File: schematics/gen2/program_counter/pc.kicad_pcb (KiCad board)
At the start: 2 copper layers, 100 x 91 mm, 18 parts, among them U1 74HC00, U2 74HC193, U3 74HC193, U4 74HC193, U5 74HC193, U6 74HC245, U7 74HC245

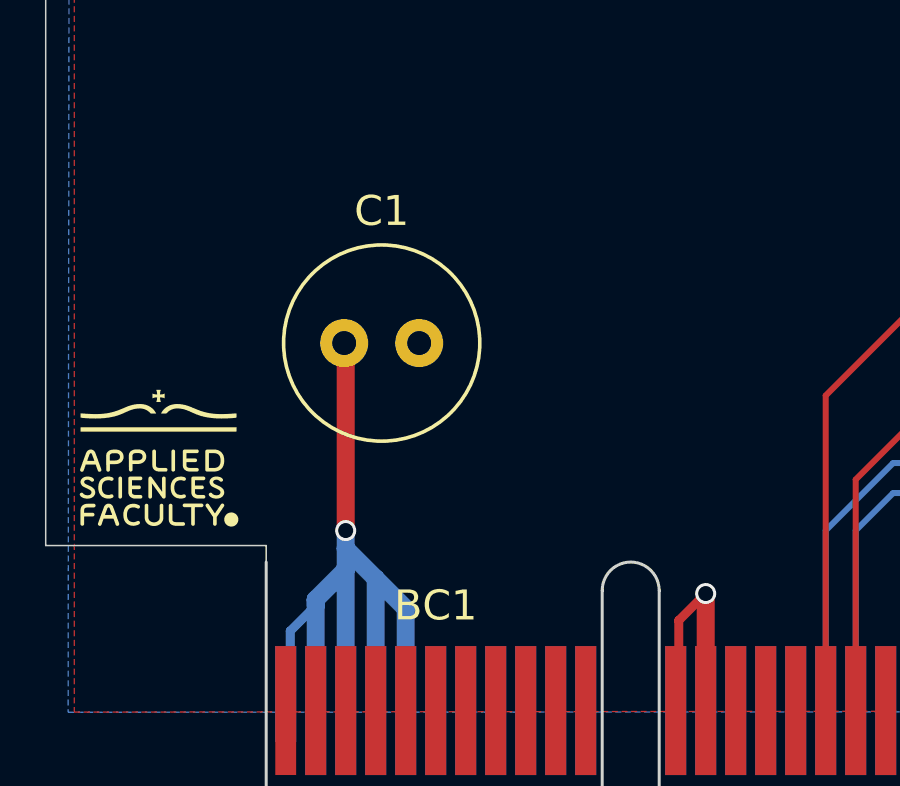
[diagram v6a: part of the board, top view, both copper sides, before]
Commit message: changes pc sc interface
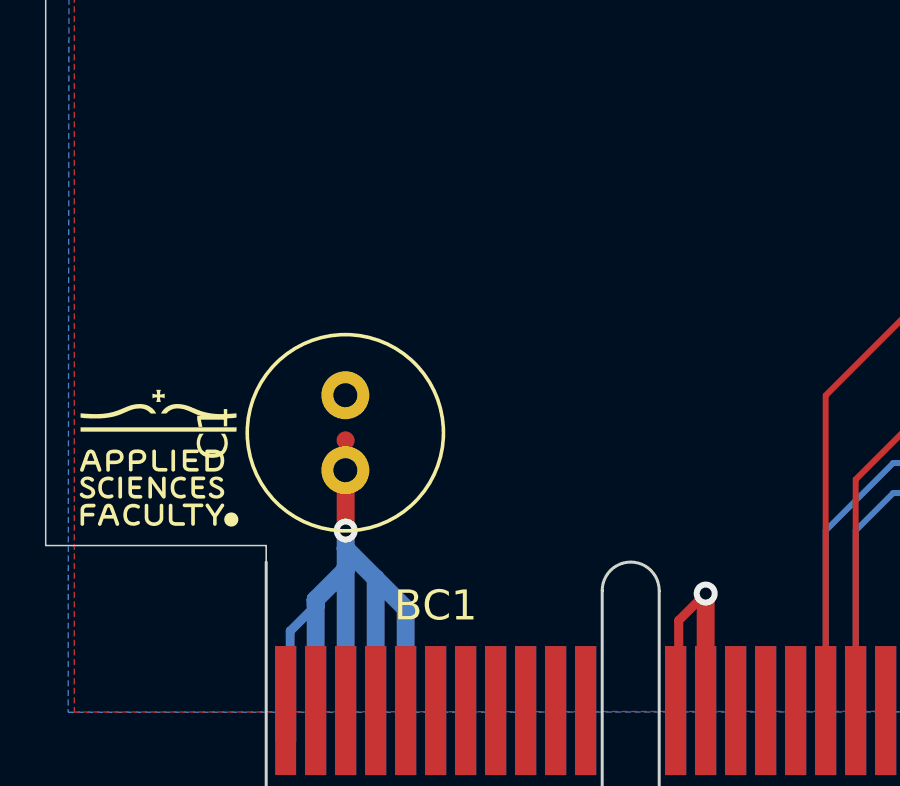
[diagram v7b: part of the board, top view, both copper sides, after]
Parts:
- moved C1 4.24 mm to (116.5, 122.0), turned to 90 degrees
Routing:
- net VCC: track 89.5 -> 85.3 mm
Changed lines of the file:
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@@
 			(pinfunction "VCC")
 			(pintype "power_in")
+			(zone_connect 0)
 		)
 		(embedded_fonts no)
@@
 			(pinfunction "VCC")
 			(pintype "power_in")
+			(zone_connect 0)
 		)
 		(embedded_fonts no)
@@
 			(pinfunction "VCC")
 			(pintype "power_in")
+			(zone_connect 0)
 		)
 		(embedded_fonts no)
@@
 			(pinfunction "VCC")
 			(pintype "power_in")
+			(zone_connect 0)
 		)
 		(embedded_fonts no)
@@
 			(pinfunction "VCC")
 			(pintype "power_in")
+			(zone_connect 0)
 		)
 		(embedded_fonts no)
@@
 			(pinfunction "VCC")
 			(pintype "power_in")
+			(zone_connect 0)
 		)
 		(embedded_fonts no)
@@
 			(pinfunction "VCC")
 			(pintype "power_in")
+			(zone_connect 0)
 		)
 		(embedded_fonts no)
@@
 	(footprint "Capacitor_THT:C_Radial_D6.3mm_H5.0mm_P2.50mm"
 		(layer "F.Cu")
-		(at 116.45 117.75)
+		(at 116.488491 121.98901 90)
 		(descr "C, Radial series, Radial, pin pitch=2.50mm, diameter=6.3mm, height=5mm, Non-Polar Electrolytic Capacitor")
 		(tags "C Radial series Radial pin pitch 2.50mm diameter 6.3mm height 5mm Non-Polar Electrolytic Capacitor")
 		(property "Reference" "C1"
-			(at 1.25 -4.4 0)
+			(at 1.25 -4.4 90)
 			(layer "F.SilkS")
 			(effects
@@
 		)
 		(property "Value" "C"
-			(at 1.25 4.4 0)
+			(at 1.25 4.4 90)
 			(layer "F.Fab")
 			(effects
@@
 		)
 		(property "Datasheet" "~"
-			(at 0 0 0)
+			(at 0 0 90)
 			(layer "F.Fab")
 			(hide yes)
@@
 		)
 		(property "Description" "Unpolarized capacitor"
-			(at 0 0 0)
+			(at 0 0 90)
 			(layer "F.Fab")
 			(hide yes)
@@
 		)
 		(fp_text user "${REFERENCE}"
-			(at 1.25 0 0)
+			(at 1.25 0 90)
 			(layer "F.Fab")
 			(effects
@@
 		)
 		(pad "1" thru_hole circle
-			(at 0 0)
+			(at 0 0 90)
 			(size 1.6 1.6)
 			(drill 0.8)
@@
 		)
 		(pad "2" thru_hole circle
-			(at 2.5 0)
+			(at 2.5 0 90)
 			(size 1.6 1.6)
 			(drill 0.8)
@@
 	)
 	(segment
+		(start 116.5 124)
+		(end 116.5 122.000519)
+		(width 0.6)
+		(layer "F.Cu")
+		(net 1)
+	)
+	(segment
+		(start 116.5 120.998961)
+		(end 116.49351 120.992471)
+		(width 0.6)
+		(layer "F.Cu")
+		(net 1)
+	)
+	(segment
 		(start 192.5 114.95)
 		(end 192.6 115.05)
@@
 	)
 	(segment
-		(start 116.5 124)
-		(end 116.5 117.75)
-		(width 0.6)
-		(layer "F.Cu")
-		(net 1)
-	)
-	(segment
 		(start 157.684777 88.234777)
 		(end 157.2 87.75)
@@
 	)
 	(segment
+		(start 116.5 122.000519)
+		(end 116.488491 121.98901)
+		(width 0.6)
+		(layer "F.Cu")
+		(net 1)
+	)
+	(segment
 		(start 192.5 108.5)
 		(end 192.5 114.95)
@@
 	(via
 		(at 116.5 124)
-		(size 0.7)
-		(drill 0.5)
+		(size 0.8)
+		(drill 0.4)
 		(layers "F.Cu" "B.Cu")
 		(free yes)
@@
 	(via
 		(at 128.5 126.1)
-		(size 0.7)
-		(drill 0.5)
+		(size 0.8)
+		(drill 0.4)
 		(layers "F.Cu" "B.Cu")
 		(free yes)
